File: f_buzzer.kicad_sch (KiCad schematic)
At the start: 11 parts, among them J1 Conn_01x03, U1 SN74123N

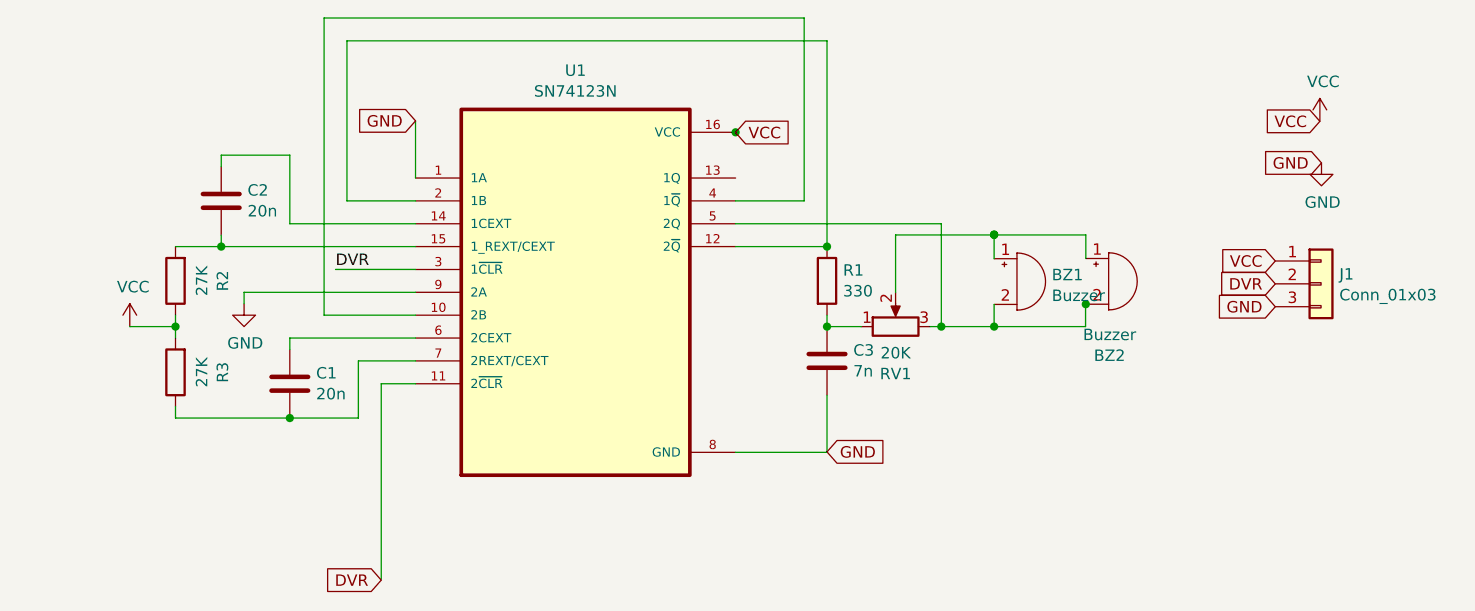
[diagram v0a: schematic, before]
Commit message: Update the footprints to SMD ones
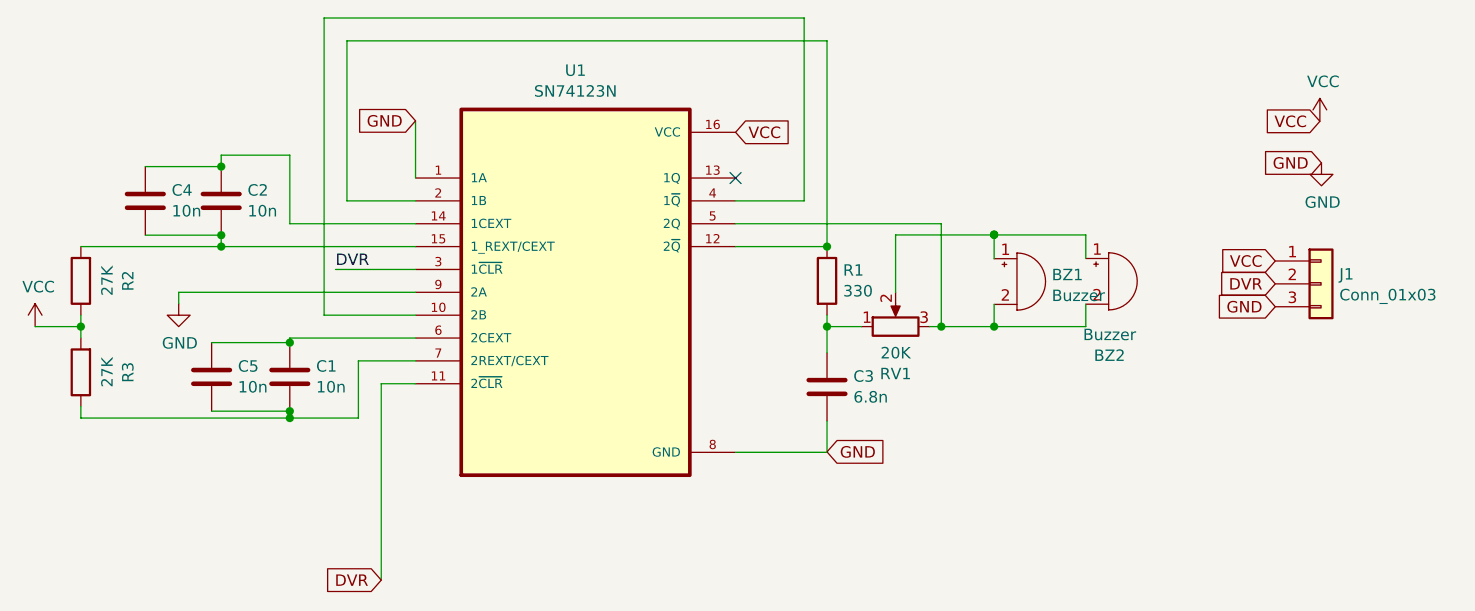
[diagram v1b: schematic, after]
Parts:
- added C4, C5: 10n, Capacitor_SMD:C_0402_1005Metric, symbol Device:C
- C1, C2: value 20n -> 10n; footprint Capacitor_THT:C_Disc_D5.1mm_W3.2mm_P5.00mm -> Capacitor_SMD:C_0402_1005Metric
- C3: value 7n -> 6.8n; footprint Capacitor_THT:C_Disc_D5.1mm_W3.2mm_P5.00mm -> Capacitor_SMD:C_0402_1005Metric
- R1, R2, R3: footprint Resistor_THT:R_Axial_DIN0207_L6.3mm_D2.5mm_P7.62mm_Horizontal -> Resistor_SMD:R_0402_1005Metric
- U1: footprint Package_DIP:DIP-16_W7.62mm -> Package_SO:SOIC-16_3.9x9.9mm_P1.27mm
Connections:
- net VCC: now also U1.16 (VCC)
- net at C1.2, R3.1, U1.7 (2REXT/CEXT): now also C5.2
- net at C2.2, R2.2, U1.15 (1_REXT/CEXT): now also C4.2
- net at C1.1, U1.6 (2CEXT): now also C5.1
- net at C2.1, U1.14 (1CEXT): now also C4.1
- net at BZ2.2 (+): now also BZ1.2 (+), RV1.3, U1.5 (2Q)
- no-connect marks 0 -> 1
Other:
- moved on the sheet: C1, C3, R2, R3
